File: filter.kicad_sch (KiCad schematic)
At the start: 17 parts, among them U301 RS8752XK, U302 RS8752XK

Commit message: schematic/pcb update
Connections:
- no-connect marks 0 -> 3
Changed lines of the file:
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@@
   (junction (at 132.08 104.14) (diameter 0) (color 0 0 0 0)
   )
+  (no_connect (at 67.31 88.9))
+  (no_connect (at 67.31 83.82))
+  (no_connect (at 153.67 88.9))
   (wire (pts (xy 149.86 60.96) (xy 132.08 60.96))
     (stroke (width 0) (type default) (color 0 0 0 0))
@@
   (symbol (lib_id "power:GND") (at 121.92 53.34 0) (unit 1)
     (in_bom yes) (on_board yes) (fields_autoplaced)
-    (property "Reference" "#PWR0306" (id 0) (at 121.92 59.69 0)
+    (property "Reference" "#PWR0304" (id 0) (at 121.92 59.69 0)
       (effects (font (size 1.27 1.27)) hide)
     )
@@
   (symbol (lib_id "power:GND") (at 57.15 50.8 0) (unit 1)
     (in_bom yes) (on_board yes) (fields_autoplaced)
-    (property "Reference" "#PWR0304" (id 0) (at 57.15 57.15 0)
+    (property "Reference" "#PWR0302" (id 0) (at 57.15 57.15 0)
       (effects (font (size 1.27 1.27)) hide)
     )
@@
   (symbol (lib_id "power:GND") (at 170.18 53.34 0) (unit 1)
     (in_bom yes) (on_board yes) (fields_autoplaced)
-    (property "Reference" "#PWR0302" (id 0) (at 170.18 59.69 0)
+    (property "Reference" "#PWR0305" (id 0) (at 170.18 59.69 0)
       (effects (font (size 1.27 1.27)) hide)
     )
@@
   (symbol (lib_id "power:GND") (at 96.52 53.34 0) (unit 1)
     (in_bom yes) (on_board yes) (fields_autoplaced)
-    (property "Reference" "#PWR0305" (id 0) (at 96.52 59.69 0)
+    (property "Reference" "#PWR0303" (id 0) (at 96.52 59.69 0)
       (effects (font (size 1.27 1.27)) hide)
     )
@@
   (symbol (lib_id "power:GND") (at 181.61 53.34 0) (unit 1)
     (in_bom yes) (on_board yes) (fields_autoplaced)
-    (property "Reference" "#PWR0303" (id 0) (at 181.61 59.69 0)
-      (effects (font (size 1.27 1.27)) hide)
-    )
+    (property "Reference" "#PWR0306" (id 0) (at 181.61 59.69 0)
+      (effects (font (size 1.27 1.27)) hide)
+    )

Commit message: schematic/pcb update
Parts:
- C302, C303, C304, C306, C307, C308: footprint (none) -> Capacitor_SMD:C_0603_1608Metric
- R301, R302, R303, R304, R305, R306, R307: footprint (none) -> Resistor_SMD:R_0603_1608Metric
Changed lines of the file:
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@@
     (stroke (width 0) (type default) (color 0 0 0 0))
+  )
+  (global_label "TX_FLAT" (shape input) (at 156.21 46.99 0) (fields_autoplaced)
+    (effects (font (size 1.27 1.27)) (justify left))
+    (property "Intersheet References" "${INTERSHEET_REFS}" (id 0) (at 165.9407 47.0694 0)
+      (effects (font (size 1.27 1.27)) (justify left) hide)
+    )
   )
   (global_label "ADC1" (shape input) (at 153.67 88.9 0) (fields_autoplaced)
@@
     )
   )
+  (global_label "TX_NF" (shape input) (at 156.21 50.8 0) (fields_autoplaced)
+    (effects (font (size 1.27 1.27)) (justify left))
+    (property "Intersheet References" "${INTERSHEET_REFS}" (id 0) (at 164.1869 50.8794 0)
+      (effects (font (size 1.27 1.27)) (justify left) hide)
+    )
+  )
   (global_label "DAC1" (shape input) (at 54.61 40.64 180) (fields_autoplaced)
     (effects (font (size 1.27 1.27)) (justify right))
@@
     )
   )
+  (global_label "RX_FLAT" (shape input) (at 41.91 88.9 0) (fields_autoplaced)
+    (effects (font (size 1.27 1.27)) (justify left))
+    (property "Intersheet References" "${INTERSHEET_REFS}" (id 0) (at 51.9431 88.9794 0)
+      (effects (font (size 1.27 1.27)) (justify left) hide)
+    )
+  )
   (symbol (lib_id "power:GND") (at 96.52 96.52 0) (unit 1)
     (in_bom yes) (on_board yes) (fields_autoplaced)
@@
     (property "Reference" "R306" (id 0) (at 102.87 80.01 90))
     (property "Value" "4.7k" (id 1) (at 102.87 82.55 90))
-    (property "Footprint" "" (id 2) (at 102.87 88.138 90)
+    (property "Footprint" "Resistor_SMD:R_0603_1608Metric" (id 2) (at 102.87 88.138 90)
       (effects (font (size 1.27 1.27)) hide)
     )
@@
       (effects (font (size 1.27 1.27)) (justify left))
     )
-    (property "Footprint" "" (id 2) (at 110.1852 52.07 0)
+    (property "Footprint" "Capacitor_SMD:C_0603_1608Metric" (id 2) (at 110.1852 52.07 0)
       (effects (font (size 1.27 1.27)) hide)
     )
@@
     (property "Reference" "R301" (id 0) (at 90.17 36.83 90))
     (property "Value" "5.1k" (id 1) (at 90.17 39.37 90))
-    (property "Footprint" "" (id 2) (at 90.17 44.958 90)
+    (property "Footprint" "Resistor_SMD:R_0603_1608Metric" (id 2) (at 90.17 44.958 90)
       (effects (font (size 1.27 1.27)) hide)
     )
@@
     (property "Reference" "R303" (id 0) (at 115.57 36.83 90))
     (property "Value" "4.7k" (id 1) (at 115.57 39.37 90))
-    (property "Footprint" "" (id 2) (at 115.57 44.958 90)
+    (property "Footprint" "Resistor_SMD:R_0603_1608Metric" (id 2) (at 115.57 44.958 90)
       (effects (font (size 1.27 1.27)) hide)
     )
@@
       (effects (font (size 1.27 1.27)) (justify right))
     )
-    (property "Footprint" "" (id 2) (at 58.928 45.72 90)
+    (property "Footprint" "Resistor_SMD:R_0603_1608Metric" (id 2) (at 58.928 45.72 90)
       (effects (font (size 1.27 1.27)) hide)
     )
@@
       (effects (font (size 1.27 1.27)) (justify left))
     )
-    (property "Footprint" "" (id 2) (at 97.4852 52.07 0)
+    (property "Footprint" "Capacitor_SMD:C_0603_1608Metric" (id 2) (at 97.4852 52.07 0)
       (effects (font (size 1.27 1.27)) hide)
     )
@@
       (effects (font (size 1.27 1.27)) (justify left))
     )
-    (property "Footprint" "" (id 2) (at 122.8852 95.25 0)
+    (property "Footprint" "Capacitor_SMD:C_0603_1608Metric" (id 2) (at 122.8852 95.25 0)
       (effects (font (size 1.27 1.27)) hide)
     )
@@
     (property "Reference" "R307" (id 0) (at 115.57 80.01 90))
     (property "Value" "4.7k" (id 1) (at 115.57 82.55 90))
-    (property "Footprint" "" (id 2) (at 115.57 88.138 90)
+    (property "Footprint" "Resistor_SMD:R_0603_1608Metric" (id 2) (at 115.57 88.138 90)
       (effects (font (size 1.27 1.27)) hide)
     )
@@
       (effects (font (size 1.27 1.27)) (justify left))
     )
-    (property "Footprint" "" (id 2) (at 97.4852 95.25 0)
+    (property "Footprint" "Capacitor_SMD:C_0603_1608Metric" (id 2) (at 97.4852 95.25 0)
       (effects (font (size 1.27 1.27)) hide)
     )
@@
       (effects (font (size 1.27 1.27)) (justify left))
     )
-    (property "Footprint" "" (id 2) (at 122.8852 52.07 0)
+    (property "Footprint" "Capacitor_SMD:C_0603_1608Metric" (id 2) (at 122.8852 52.07 0)
       (effects (font (size 1.27 1.27)) hide)
     )
@@
     (property "Reference" "R305" (id 0) (at 90.17 80.01 90))
     (property "Value" "5.1k" (id 1) (at 90.17 82.55 90))
-    (property "Footprint" "" (id 2) (at 90.17 88.138 90)
+    (property "Footprint" "Resistor_SMD:R_0603_1608Metric" (id 2) (at 90.17 88.138 90)
       (effects (font (size 1.27 1.27)) hide)
     )
@@
     (property "Reference" "R302" (id 0) (at 102.87 36.83 90))
     (property "Value" "4.7k" (id 1) (at 102.87 39.37 90))
-    (property "Footprint" "" (id 2) (at 102.87 44.958 90)
+    (property "Footprint" "Resistor_SMD:R_0603_1608Metric" (id 2) (at 102.87 44.958 90)
       (effects (font (size 1.27 1.27)) hide)
     )
@@
       (effects (font (size 1.27 1.27)) (justify left))
     )
-    (property "Footprint" "" (id 2) (at 110.1852 95.25 0)
-      (effects (font (size 1.27 1.27)) hide)
-    )
+    (property "Footprint" "Capacitor_SMD:C_0603_1608Metric" (id 2) (at 110.1852 95.25 0)
+      (effects (font (size 1.27 1.27)) hide)
+    )

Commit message: schematic/pcb update
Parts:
- added C309, C310, C311, C312, C313, C314, C315: 10u, Capacitor_SMD:C_0603_1608Metric, symbol Device:C
- added R308, R309, R310, R311, R312, R313, R314, R315: 4.7k, Resistor_SMD:R_0603_1608Metric, symbol Device:R
- added RV301, RV302: 50k, Potentiometer_SMD:Potentiometer_Bourns_TC33X_Vertical, symbol Device:R_Potentiometer
- R304: value 10k -> 4.7k
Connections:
- net +3V3: now also R310.2
- net ADC1: now also C307.2, U302.6 (-), U302.7
- net GND: now also C314.2, C315.2, R309.1, R313.1, RV301.1
- net RX_FLAT: now also C312.1
- net TX_FLAT: now also C310.2
- net TX_NF: now also C311.2
- net at C303.2, U301.6 (-), U301.7: now also C309.1
- net at R305.1, U302.1: now also R314.2, RV302.1
- net at U302.2 (-): now also R314.1, R315.2, RV302.2
- net at U302.3 (+): now also C312.2, C313.2, R311.2
- new net: C314.1, R310.1, R311.1, R313.2
- new net: R312.2, R315.1, RV302.3
- new net: C315.1, R312.1
- new net: C310.1, C311.1, R308.1, R309.2, RV301.2
- new net: C309.2, R308.2, RV301.3
- new net RX_NF: C313.1
- no-connect marks 3 -> 0
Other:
- moved on the sheet: C301, C305, C306, C307, C308, R305, R306, R307, U301C, U302A, U302B, U302C

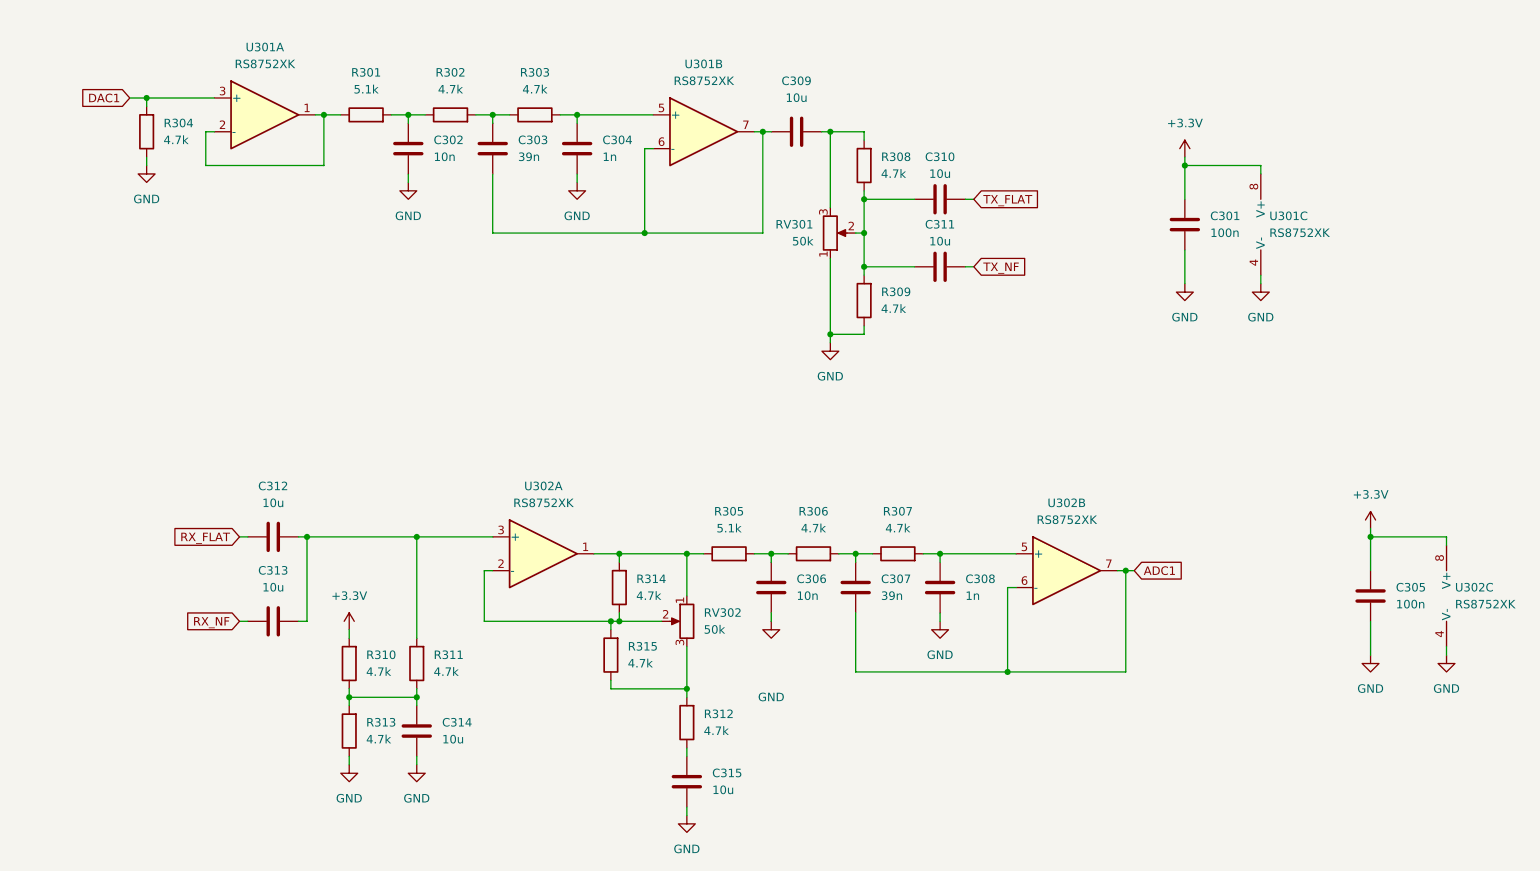
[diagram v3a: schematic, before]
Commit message: Finished schematic (BOM consolidation, LCSC part numbers) + sheet comments
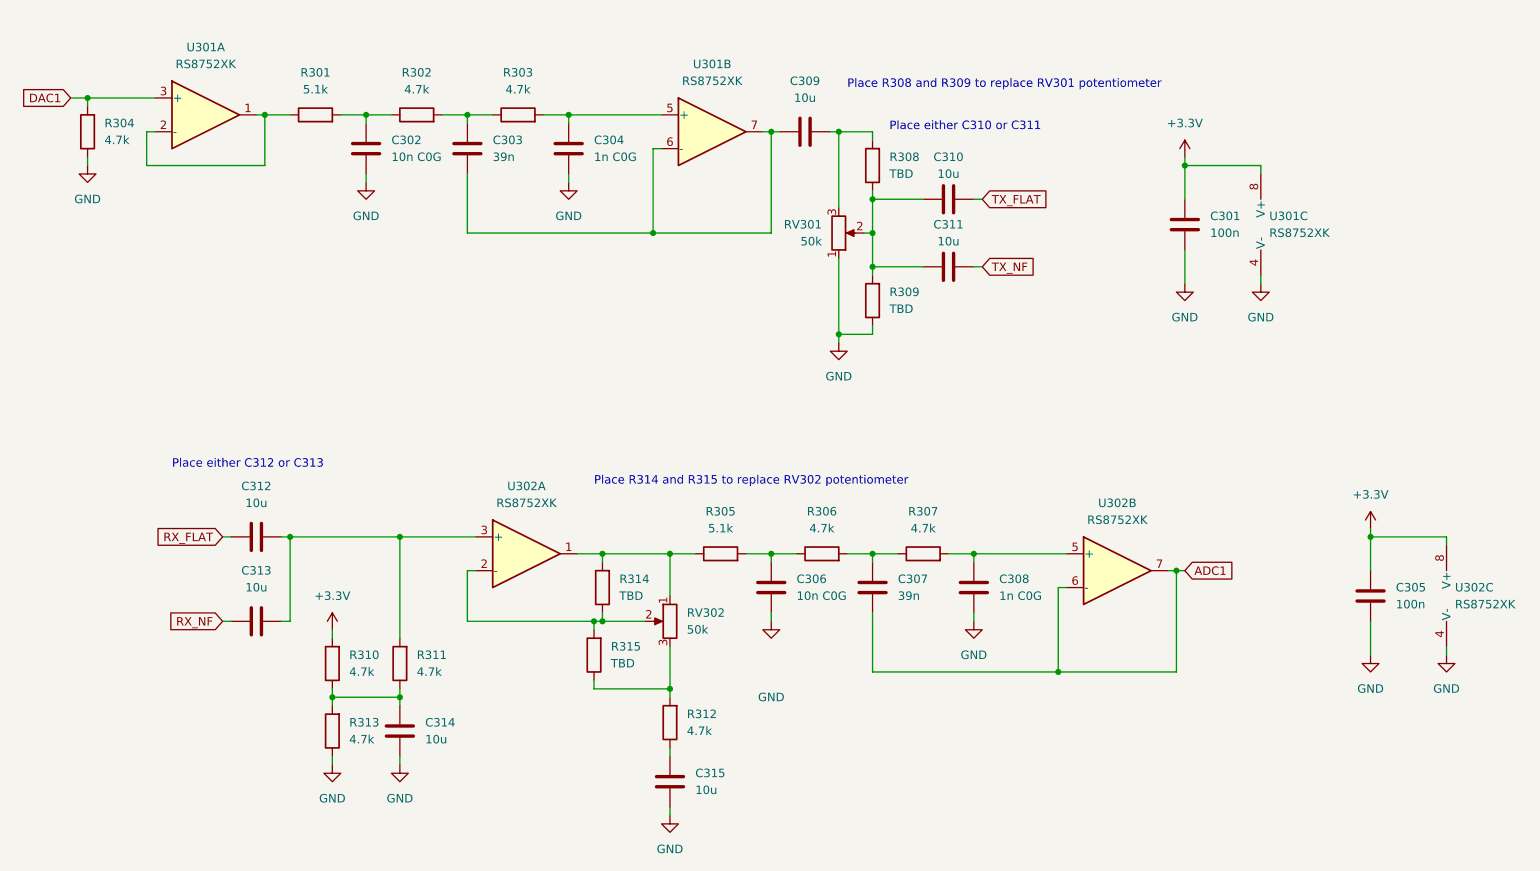
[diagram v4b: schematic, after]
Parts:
- C301, C305: LCSC (none) -> C14663
- C302, C306: value 10n -> 10n C0G; LCSC (none) -> C389113
- C303, C307: LCSC (none) -> C107091
- C304, C308: value 1n -> 1n C0G; LCSC (none) -> C106246
- C309, C310, C311, C312, C313, C314, C315: LCSC (none) -> C2922482
- R301, R305: LCSC (none) -> C23186
- R302, R303, R304, R306, R307, R310, R311, R312, R313: LCSC (none) -> C105428
- R308, R309, R314, R315: value 4.7k -> TBD
- U301, U302: footprint (none) -> Package_SO:SOIC-8_3.9x4.9mm_P1.27mm; LCSC (none) -> C236994
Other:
- note added: "Place R308 and R309 to replace RV301 potentiometer"
- note added: "Place R314 and R315 to replace RV302 potentiometer"
- note added: "Place either C310 or C311"
- note added: "Place either C312 or C313"
- company: (none) -> Robin Olejnik
- title: (none) -> Bosch KF163 control
- moved on the sheet: C302, C303, C304, C307, C308, C309, C310, C311, C312, C313, C314, C315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
